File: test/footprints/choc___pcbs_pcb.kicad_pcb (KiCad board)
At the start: 2 copper layers, 5 parts

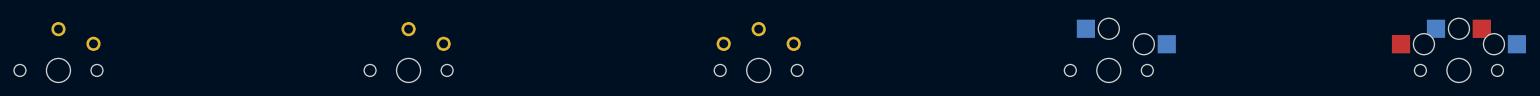
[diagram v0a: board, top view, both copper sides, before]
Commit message: TEST: Fix tests for new power netclass
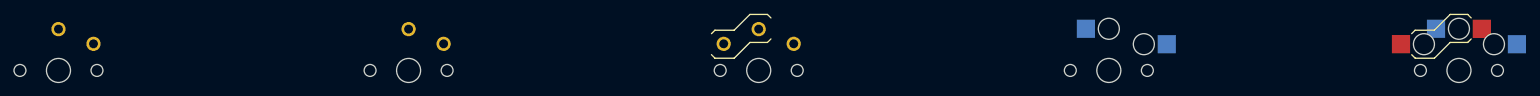
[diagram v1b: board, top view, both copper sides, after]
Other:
- net class Power added: clearance 0.2, trace_width 0.5, via_dia 0.8, via_drill 0.4
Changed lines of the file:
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@@
 (add_net "to")
   )
-      (module PG1350 (layer F.Cu)
+  (net_class Power "This is the power net class."
+    (clearance 0.2)
+    (trace_width 0.5)
+    (via_dia 0.8)
+    (via_drill 0.4)
+    (uvia_dia 0.3)
+    (uvia_drill 0.1)
+  )
+      (footprint PG1350 (layer F.Cu)
+      (attr through_hole)
       (at 0 0 0)
       (fp_text reference "S1" (at 0 0) (layer F.SilkS) hide (effects (font (size 1.27 1.27) (thickness 0.15))))
@@
             (pad 1 thru_hole circle (at 5 -3.8) (size 2.032 2.032) (drill 1.27) (layers *.Cu *.Mask) (net 1 "from"))
             (pad 2 thru_hole circle (at 0 -5.9) (size 2.032 2.032) (drill 1.27) (layers *.Cu *.Mask) (net 2 "to"))
-          )
-      (module PG1350 (layer F.Cu)
+        (model ${KICAD6_3RD_PARTY}/3dmodels/ergogen/SW_Kailh_Choc_V1.stp
+              (at (xyz 0 0 0))
+              (scale (xyz 1 1 1))
+              (rotate (xyz 0 0 0))
+        )
+        )
+      (footprint PG1350 (layer F.Cu)
+      (attr through_hole)
       (at 50 0 0)
       (fp_text reference "S2" (at 0 0) (layer F.SilkS) hide (effects (font (size 1.27 1.27) (thickness 0.15))))
@@
             (pad 1 thru_hole circle (at 5 -3.8) (size 2.032 2.032) (drill 1.27) (layers *.Cu *.Mask) (net 1 "from"))
             (pad 2 thru_hole circle (at 0 -5.9) (size 2.032 2.032) (drill 1.27) (layers *.Cu *.Mask) (net 2 "to"))
+          (model ${KICAD6_3RD_PARTY}/3dmodels/ergogen/MBK_Keycap_-_1u.step
+              (at (xyz -9.999999999177334e-7 0 0.25))
+              (scale (xyz 1 1 1))
+              (rotate (xyz 0 0 0))
           )
-      (module PG1350 (layer F.Cu)
+        (model ${KICAD6_3RD_PARTY}/3dmodels/ergogen/SW_Kailh_Choc_V1.stp
+              (at (xyz 0 0 0))
+              (scale (xyz 1 1 1))
+              (rotate (xyz 0 0 0))
+        )
+        )
+      (footprint PG1350 (layer F.Cu)
+      (attr through_hole)
       (at 100 0 0)
       (fp_text reference "S3" (at 0 0) (layer F.SilkS) hide (effects (font (size 1.27 1.27) (thickness 0.15))))
@@
             (pad 1 thru_hole circle (at -5 -3.8) (size 2.032 2.032) (drill 1.27) (layers *.Cu *.Mask) (net 1 "from"))
             (pad 2 thru_hole circle (at -0 -5.9) (size 2.032 2.032) (drill 1.27) (layers *.Cu *.Mask) (net 2 "to"))
-          )
-      (module PG1350 (layer F.Cu)
+    (fp_line (start 1.25 -8) (end -1.25 -8) (layer "F.SilkS") (width 0.12))
+    (fp_line (start -6.25 -5.75) (end -6.75 -5.25) (layer "F.SilkS") (width 0.12))
+    (fp_line (start 1.75 -7.5) (end 1.25 -8) (layer "F.SilkS") (width 0.12))
+    (fp_line (start -3.5 -1.75) (end -1.25 -4) (layer "F.SilkS") (width 0.12))
+    (fp_line (start 1.25 -4) (end 1.75 -4.5) (layer "F.SilkS") (width 0.12))
+    (fp_line (start -6.25 -1.75) (end -3.5 -1.75) (layer "F.SilkS") (width 0.12))
+    (fp_line (start -1.25 -4) (end 1.25 -4) (layer "F.SilkS") (width 0.12))
+    (fp_line (start -3.5 -5.75) (end -6.25 -5.75) (layer "F.SilkS") (width 0.12))
+    (fp_line (start -1.25 -8) (end -3.5 -5.75) (layer "F.SilkS") (width 0.12))
+    (fp_line (start -6.75 -2.25) (end -6.25 -1.75) (layer "F.SilkS") (width 0.12))
+        (model ${KICAD6_3RD_PARTY}/3dmodels/ergogen/SW_Kailh_Choc_V1.stp
+              (at (xyz 0 0 0))
+              (scale (xyz 1 1 1))
+              (rotate (xyz 0 0 0))
+        )
+        )
+      (footprint PG1350 (layer F.Cu)
+      (attr through_hole)
       (at 150 0 0)
       (fp_text reference "S4" (at 0 0) (layer F.SilkS) hide (effects (font (size 1.27 1.27) (thickness 0.15))))
@@
       (pad "" np_thru_hole circle (at 5.5 0) (size 1.7018 1.7018) (drill 1.7018) (layers *.Cu *.Mask))
       (pad "" np_thru_hole circle (at -5.5 0) (size 1.7018 1.7018) (drill 1.7018) (layers *.Cu *.Mask))
+    (fp_line (start 6.25 -5.75) (end 6.75 -5.25) (layer "B.SilkS") (width 0.12))
+    (fp_line (start 3.5 -5.75) (end 6.25 -5.75) (layer "B.SilkS") (width 0.12))
+    (fp_line (start 6.75 -2.25) (end 6.25 -1.75) (layer "B.SilkS") (width 0.12))
+    (fp_line (start 6.25 -1.75) (end 3.5 -1.75) (layer "B.SilkS") (width 0.12))
+    (fp_line (start -1.75 -7.5) (end -1.25 -8) (layer "B.SilkS") (width 0.12))
+    (fp_line (start 3.5 -1.75) (end 1.25 -4) (layer "B.SilkS") (width 0.12))
+    (fp_line (start 1.25 -4) (end -1.25 -4) (layer "B.SilkS") (width 0.12))
+    (fp_line (start 1.25 -8) (end 3.5 -5.75) (layer "B.SilkS") (width 0.12))
+    (fp_line (start -1.25 -8) (end 1.25 -8) (layer "B.SilkS") (width 0.12))
+    (fp_line (start -1.25 -4) (end -1.75 -4.5) (layer "B.SilkS") (width 0.12))
           (pad "" np_thru_hole circle (at 5 -3.75) (size 3 3) (drill 3) (layers *.Cu *.Mask))
           (pad "" np_thru_hole circle (at 0 -5.95) (size 3 3) (drill 3) (layers *.Cu *.Mask))
           (pad 1 smd rect (at -3.275 -5.95 0) (size 2.6 2.6) (layers B.Cu B.Paste B.Mask)  (net 1 "from"))
           (pad 2 smd rect (at 8.275 -3.75 0) (size 2.6 2.6) (layers B.Cu B.Paste B.Mask)  (net 2 "to"))
-        )
-      (module PG1350 (layer F.Cu)
+          (model ${KICAD6_3RD_PARTY}/3dmodels/ergogen/PG1350-socket.STEP
+              (at (xyz -0.21 0.15 -0.07))
+              (scale (xyz 1 1 1))
+              (rotate (xyz -90 0 180))
+          )
+        (model ${KICAD6_3RD_PARTY}/3dmodels/ergogen/SW_Kailh_Choc_V1.stp
+              (at (xyz 0 0 0))
+              (scale (xyz 1 1 1))
+              (rotate (xyz 0 0 0))
+        )
+        )
+      (footprint PG1350 (layer F.Cu)
+      (attr through_hole)
       (at 200 0 0)
       (fp_text reference "S5" (at 0 0) (layer F.SilkS) hide (effects (font (size 1.27 1.27) (thickness 0.15))))
@@
       (pad "" np_thru_hole circle (at 5.5 0) (size 1.7018 1.7018) (drill 1.7018) (layers *.Cu *.Mask))
       (pad "" np_thru_hole circle (at -5.5 0) (size 1.7018 1.7018) (drill 1.7018) (layers *.Cu *.Mask))
+    (fp_line (start 6.25 -5.75) (end 6.75 -5.25) (layer "B.SilkS") (width 0.12))
+    (fp_line (start 3.5 -5.75) (end 6.25 -5.75) (layer "B.SilkS") (width 0.12))
+    (fp_line (start 6.75 -2.25) (end 6.25 -1.75) (layer "B.SilkS") (width 0.12))
+    (fp_line (start 6.25 -1.75) (end 3.5 -1.75) (layer "B.SilkS") (width 0.12))
+    (fp_line (start -1.75 -7.5) (end -1.25 -8) (layer "B.SilkS") (width 0.12))
+    (fp_line (start 3.5 -1.75) (end 1.25 -4) (layer "B.SilkS") (width 0.12))
+    (fp_line (start 1.25 -4) (end -1.25 -4) (layer "B.SilkS") (width 0.12))
+    (fp_line (start 1.25 -8) (end 3.5 -5.75) (layer "B.SilkS") (width 0.12))
+    (fp_line (start -1.25 -8) (end 1.25 -8) (layer "B.SilkS") (width 0.12))
+    (fp_line (start -1.25 -4) (end -1.75 -4.5) (layer "B.SilkS") (width 0.12))
           (pad "" np_thru_hole circle (at 5 -3.75) (size 3 3) (drill 3) (layers *.Cu *.Mask))
           (pad "" np_thru_hole circle (at 0 -5.95) (size 3 3) (drill 3) (layers *.Cu *.Mask))
@@
           (pad 1 smd rect (at 3.275 -5.95 0) (size 2.6 2.6) (layers F.Cu F.Paste F.Mask)  (net 1 "from"))
           (pad 2 smd rect (at -8.275 -3.75 0) (size 2.6 2.6) (layers F.Cu F.Paste F.Mask)  (net 2 "to"))
+    (fp_line (start 1.25 -8) (end -1.25 -8) (layer "F.SilkS") (width 0.12))
+    (fp_line (start -6.25 -5.75) (end -6.75 -5.25) (layer "F.SilkS") (width 0.12))
+    (fp_line (start 1.75 -7.5) (end 1.25 -8) (layer "F.SilkS") (width 0.12))
+    (fp_line (start -3.5 -1.75) (end -1.25 -4) (layer "F.SilkS") (width 0.12))
+    (fp_line (start 1.25 -4) (end 1.75 -4.5) (layer "F.SilkS") (width 0.12))
+    (fp_line (start -6.25 -1.75) (end -3.5 -1.75) (layer "F.SilkS") (width 0.12))
+    (fp_line (start -1.25 -4) (end 1.25 -4) (layer "F.SilkS") (width 0.12))
+    (fp_line (start -3.5 -5.75) (end -6.25 -5.75) (layer "F.SilkS") (width 0.12))
+    (fp_line (start -1.25 -8) (end -3.5 -5.75) (layer "F.SilkS") (width 0.12))
+    (fp_line (start -6.75 -2.25) (end -6.25 -1.75) (layer "F.SilkS") (width 0.12))
+          (model ${KICAD6_3RD_PARTY}/3dmodels/ergogen/PG1350-socket.STEP
+              (at (xyz -0.21 0.15 -0.07))
+              (scale (xyz 1 1 1))
+              (rotate (xyz -90 0 180))
+          )
+        (model ${KICAD6_3RD_PARTY}/3dmodels/ergogen/SW_Kailh_Choc_V1.stp
+              (at (xyz 0 0 0))
+              (scale (xyz 1 1 1))
+              (rotate (xyz 0 0 0))
+        )
         )
 )
